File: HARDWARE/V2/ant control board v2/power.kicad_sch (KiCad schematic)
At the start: 10 parts, among them J1 USB-C_304A-ACP16X, J2 2s Battery, U2 GM7333

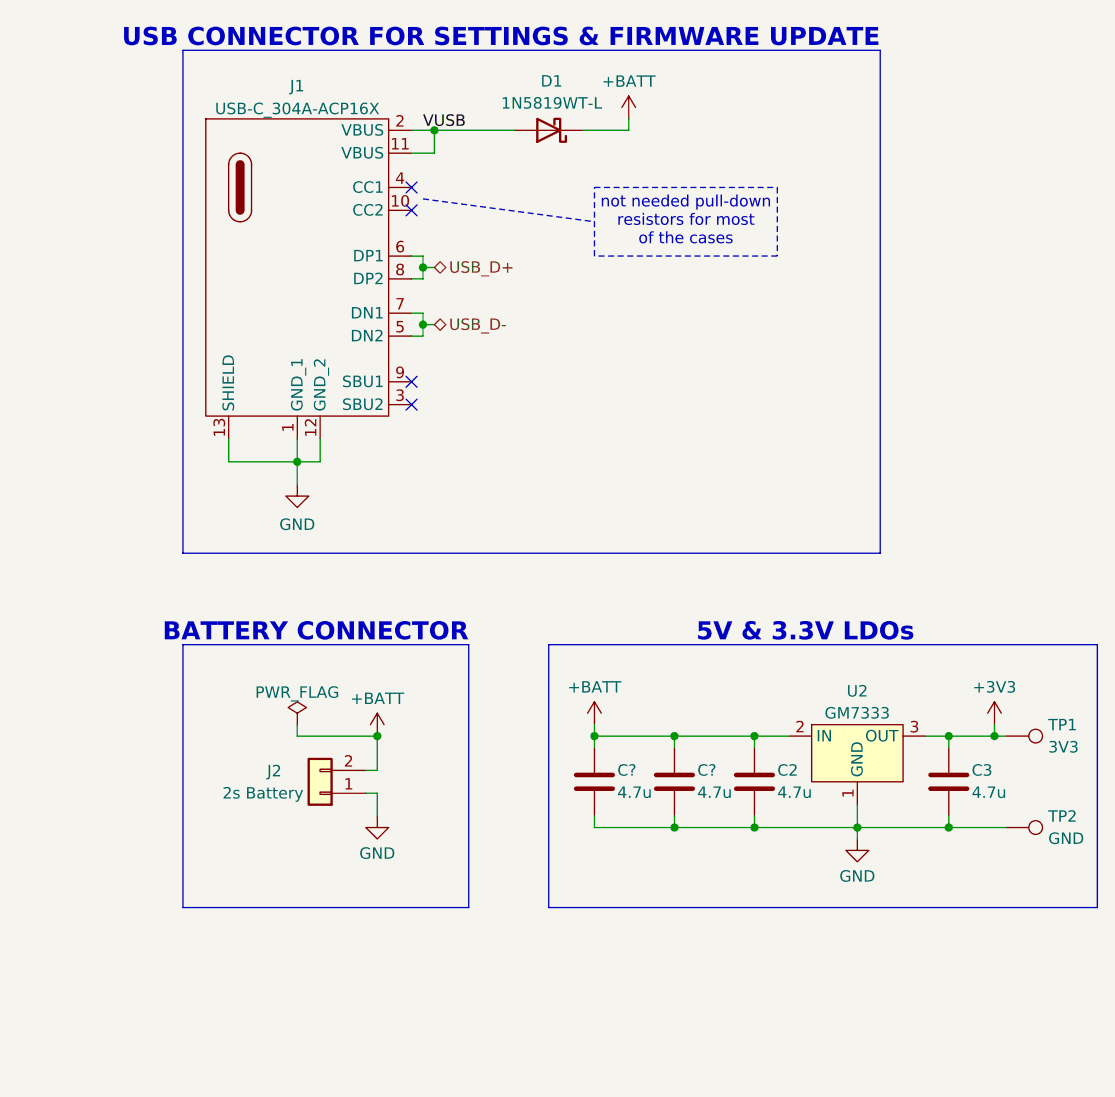
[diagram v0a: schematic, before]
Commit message: layout 2.0 facv2 done
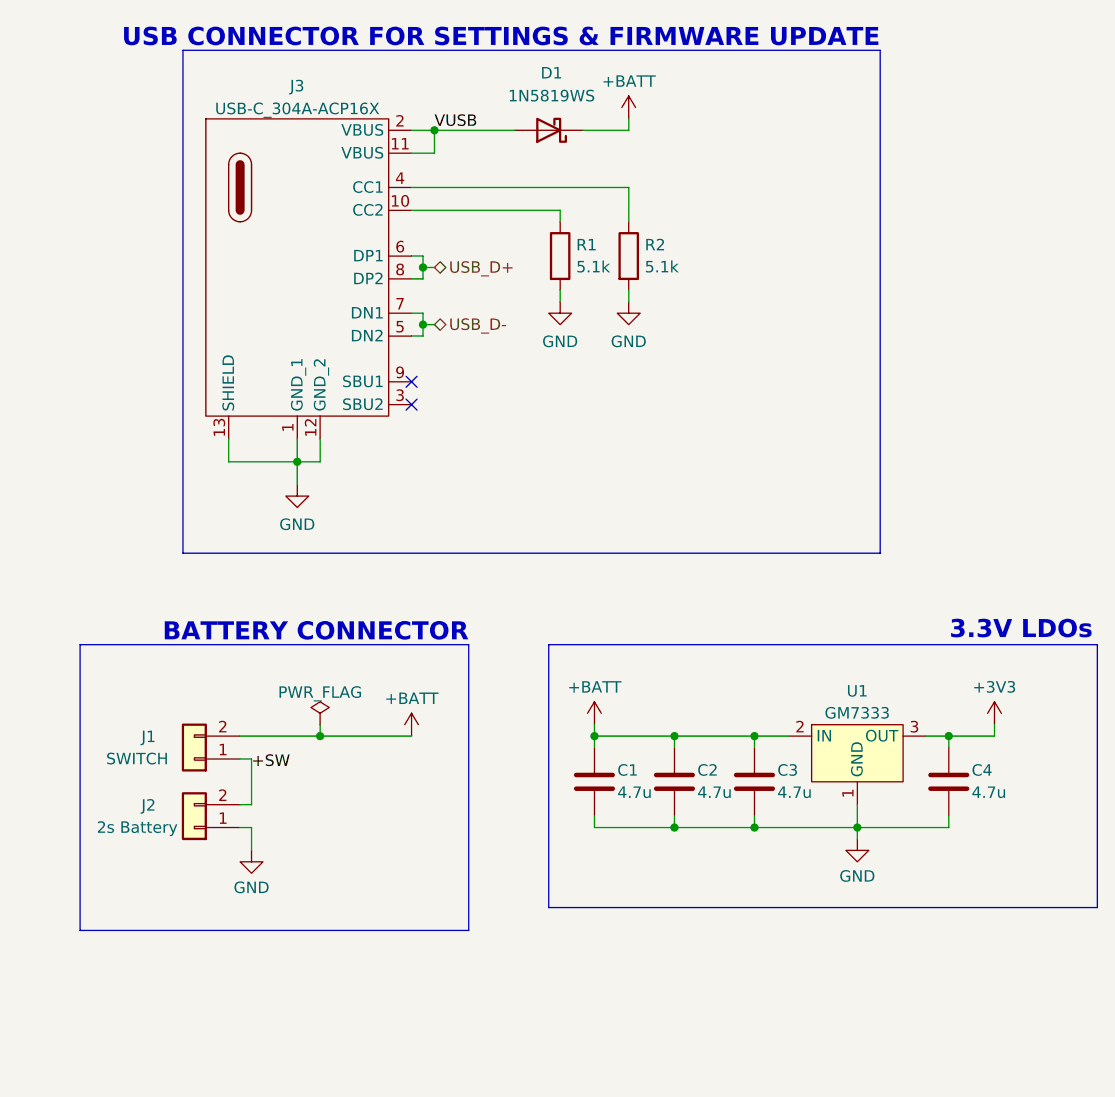
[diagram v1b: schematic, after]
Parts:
- removed TP1: 3V3, TestPoint:TestPoint_Pad_D1.0mm, symbol Connector:TestPoint
- removed TP2: GND, TestPoint:TestPoint_Pad_D1.0mm, symbol Connector:TestPoint
- added J1: SWITCH, _MY_connectors:01x02_TH_pad_renforced, symbol Connector_Generic:Conn_01x02
- added R1, R2: 5.1k, Resistor_SMD:R_0402_1005Metric, symbol Device:R
- C1, C2: renamed from C?; footprint Capacitor_SMD:C_0603_1608Metric -> Capacitor_SMD:C_0402_1005Metric
- C3: renamed from C2; footprint Capacitor_SMD:C_0603_1608Metric -> Capacitor_SMD:C_0402_1005Metric
- C4: renamed from C3; footprint Capacitor_SMD:C_0603_1608Metric -> Capacitor_SMD:C_0402_1005Metric
- D1: value 1N5819WT-L -> 1N5819WS; footprint Diode_SMD:D_SOD-123 -> Diode_SMD:D_SOD-323; LCSC C181207 -> C191023
- J2: footprint _MY_connectors:Pad 02x01 -> _MY_connectors:01x02_TH_pad_renforced
- renumbered J1 to J3, U2 to U1
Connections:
- net +BATT: now also J1.2 (Pin_2); no longer J2.2 (Pin_2), U1.4 (IN)
- net GND: now also R1.2, R2.2
- net at J3.10 (CC2): now also R1.1
- net at J3.4 (CC1): now also R2.1
- new net +SW: J1.1 (Pin_1), J2.2 (Pin_2)
- no-connect marks 4 -> 2
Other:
- note added: "3.3V LDOs"
- note removed: "5V & 3.3V LDOs"
- note removed: "not needed pull-down resistors for most of the cases"
- moved on the sheet: J2

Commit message: Updated BOM, added some images
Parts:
- C1: now not fitted
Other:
- note added: "Not populated to reduce component number to 40 and enable to have 29$ PCBA offer (PCBWay) for 15 PCBs DOSE NOT AFFECT THE CORRECT WORKING"
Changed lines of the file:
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@@
+		)
+	)
+	(rectangle
+		(start 106.68 155.702)
+		(end 147.32 165.1)
+		(stroke
+			(width 0)
+			(type default)
+		)
+		(fill
+			(type none)
 		)
 	)
@@
 		)
 	)
+	(text "Not populated to reduce component\nnumber to 40 and enable to have\n29$ PCBA offer (PCBWay) for 15 PCBs\nDOSE NOT AFFECT THE CORRECT WORKING"
+		(exclude_from_sim no)
+		(at 127 160.782 0)
+		(effects
+			(font
+				(size 1.27 1.27)
+			)
+		)
+	)
 	(junction
 		(at 113.03 74.93)
@@
 			(width 0)
 			(type default)
+		)
+	)
+	(polyline
+		(pts
+			(xy 132.08 138.43) (xy 127 156.21)
+		)
+		(stroke
+			(width 0)
+			(type dot)
 		)
 	)
@@
 		(in_bom yes)
 		(on_board yes)
-		(dnp no)
+		(dnp yes)
 		(property "Reference" "C1"
 			(at 134.62 130.81 0)
